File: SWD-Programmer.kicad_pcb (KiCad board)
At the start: 4 copper layers, 50 x 22 mm, 47 parts, among them J1 USB_C_Receptacle_USB2.0, J2 USB_BOOT, J3 Conn_01x08_Pin, U1 RP2040, U10 XC6210B332MR, U2 W25Q128JVS, U3 USBLC6-2SC6, Y1 ABM8-272-T3

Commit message: Pcb cleanup
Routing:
- net GND: track 30.6 -> 33.0 mm, vias 22 -> 34

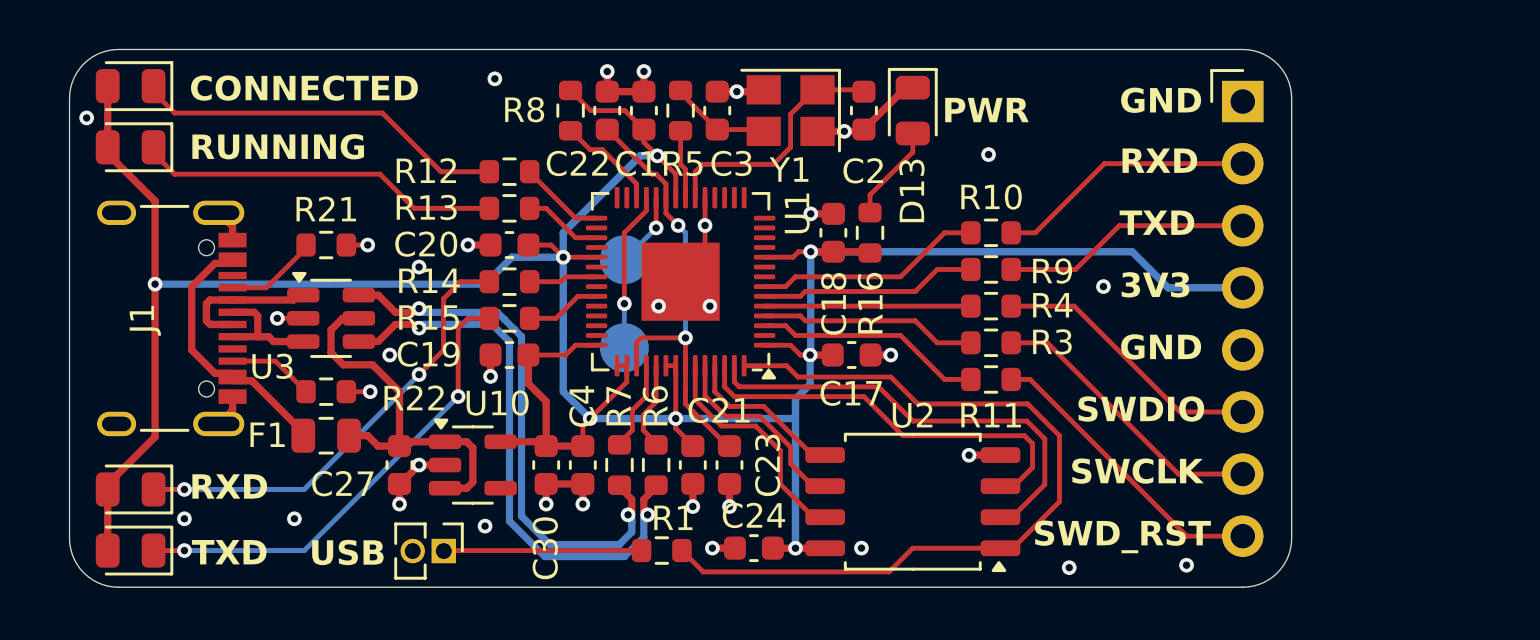
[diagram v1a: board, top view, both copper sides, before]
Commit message: Curved traces and teardrops
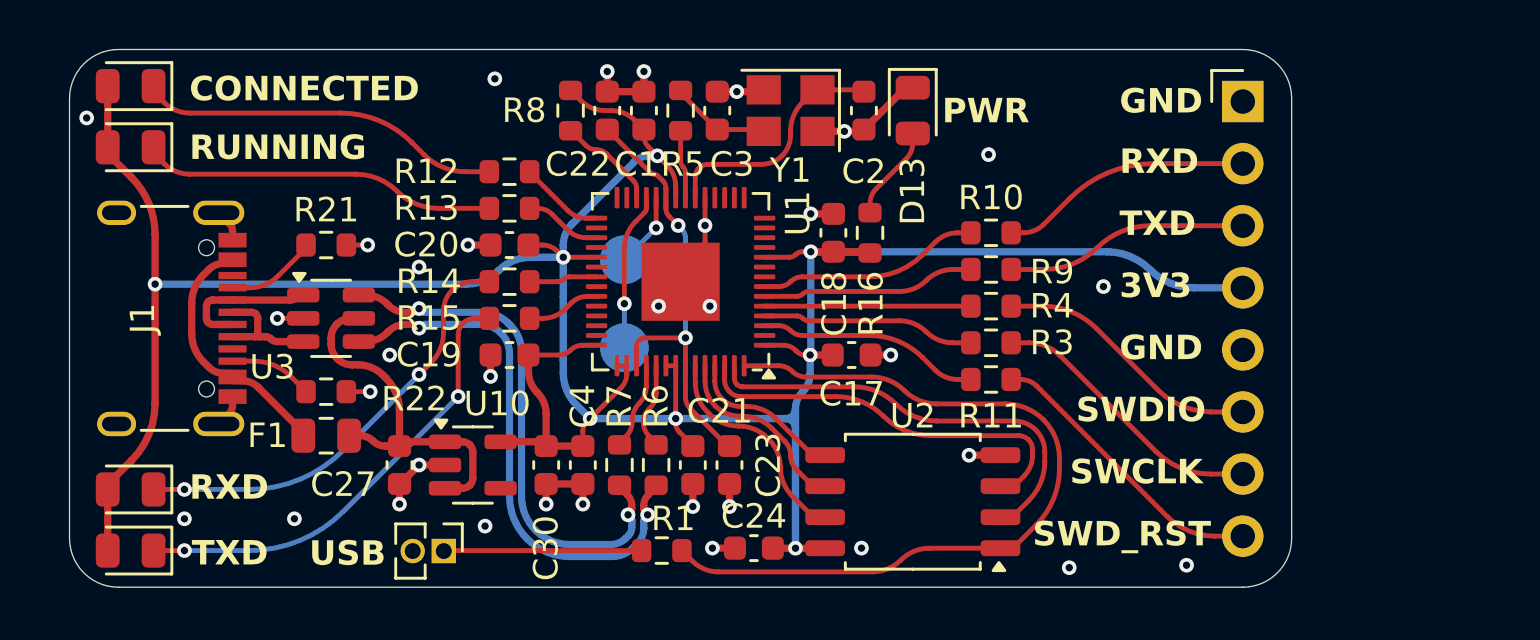
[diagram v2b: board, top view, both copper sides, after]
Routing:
- net /QSPI_SS: track 33.8 -> 32.9 mm
- net +3V3: track 128.6 -> 127.8 mm
- net /USB_D+: track 23.3 -> 22.7 mm
- net /USB_D-: track 22.5 -> 21.9 mm
- net /QSPI_SD1: track 18.6 -> 18.0 mm
